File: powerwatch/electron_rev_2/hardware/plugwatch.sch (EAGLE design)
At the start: 86 parts, among them J1 TC2030-JLINK-NL, J2 DM3AT-SF-PEJM5, SW1 SIP3240X, SW2 SIP3240X, SW3 SIP3240X, SW4 SIP3240X, SW7 SIP3240X, U1 MAX-M8, U3 ISL29035, U37 MPU-9250, U4 NRF51822QF, U5 SAFFB1G56KB0F0A, U6 BGA725L6-ALT, U7 OPA322AIDBVT, U8 MAX740XESA, X3 16MHz, X4 ABS05-32.768KHZ-9-T

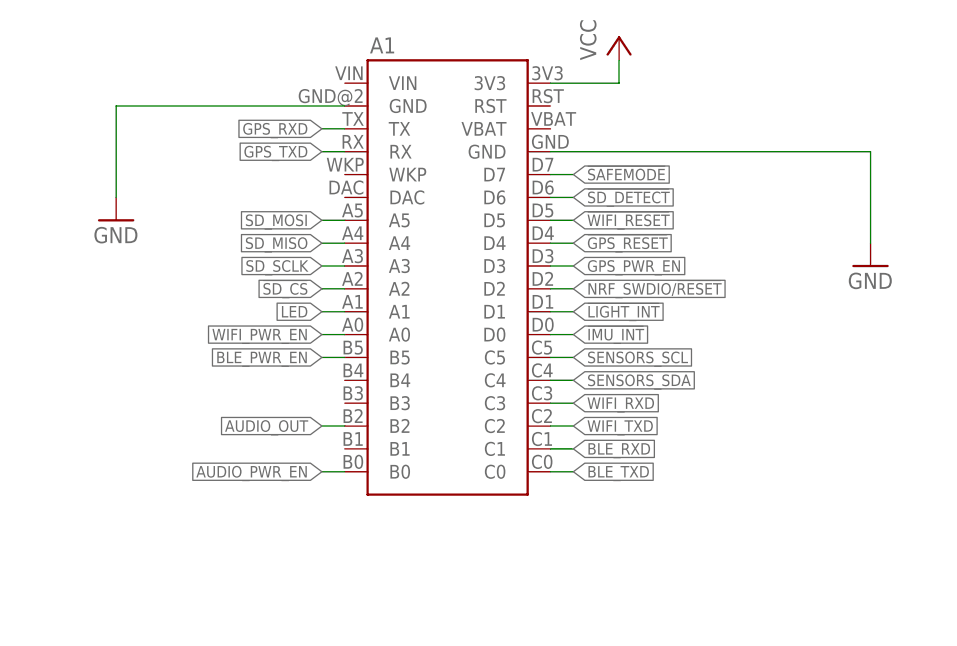
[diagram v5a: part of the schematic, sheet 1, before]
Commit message: Reroute, move signals on Electron
Add names/dates/revision
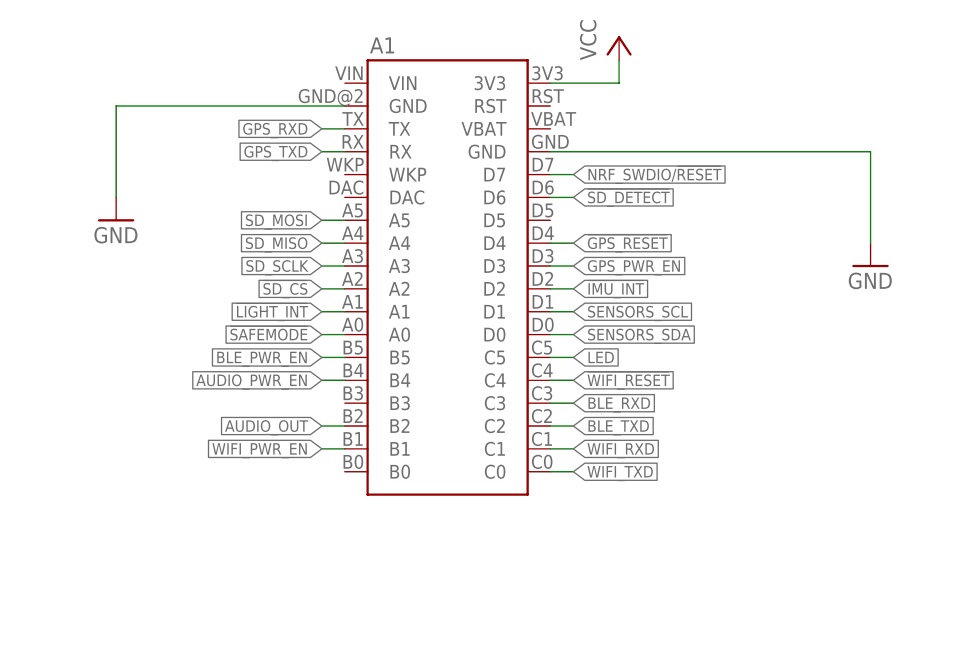
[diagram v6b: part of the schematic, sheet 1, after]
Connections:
- net !IMU_INT: now also A1.D2; no longer A1.D0
- net !LIGHT_INT: now also A1.A1; no longer A1.D1
- net !SAFEMODE: now also A1.A0; no longer A1.D7
- net !WIFI_RESET: now also A1.C4; no longer A1.D5
- net AUDIO_PWR_EN: now also A1.B4; no longer A1.B0
- net BLE_RXD: now also A1.C3; no longer A1.C1
- net BLE_TXD: now also A1.C2; no longer A1.C0
- net GPS_VCC: now also U1.V_BCKP
- net LED: now also A1.C5; no longer A1.A1
- net NRF_SWDIO/!RESET: now also A1.D7; no longer A1.D2
- net SENSORS_SCL: now also A1.D1; no longer A1.C5
- net SENSORS_SDA: now also A1.D0; no longer A1.C4
- net WIFI_PWR_EN: now also A1.B1; no longer A1.A0
- net WIFI_RXD: now also A1.C1; no longer A1.C3
- net WIFI_TXD: now also A1.C0; no longer A1.C2
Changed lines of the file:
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@@
 </segment>
+<segment>
+<wire x1="63.5" y1="119.38" x2="60.96" y2="119.38" width="0.1524" layer="91"/>
+<label x="60.96" y="119.38" size="1.27" layer="95" rot="R180" xref="yes"/>
+<pinref part="A1" gate="A1" pin="A0"/>
+</segment>
+</net>
+<net name="BLE_TXD" class="0">
+<segment>
+<label x="88.9" y="109.22" size="1.27" layer="95" xref="yes"/>
+<pinref part="A1" gate="A1" pin="C2"/>
+<wire x1="88.9" y1="109.22" x2="86.36" y2="109.22" width="0.1524" layer="91"/>
+</segment>
+</net>
+<net name="BLE_RXD" class="0">
+<segment>
+<wire x1="86.36" y1="111.76" x2="88.9" y2="111.76" width="0.1524" layer="91"/>
+<label x="88.9" y="111.76" size="1.27" layer="95" xref="yes"/>
+<pinref part="A1" gate="A1" pin="C3"/>
+</segment>
+</net>
+<net name="WIFI_TXD" class="0">
+<segment>
+<wire x1="86.36" y1="104.14" x2="88.9" y2="104.14" width="0.1524" layer="91"/>
+<label x="88.9" y="104.14" size="1.27" layer="95" xref="yes"/>
+<pinref part="A1" gate="A1" pin="C0"/>
+</segment>
+</net>
+<net name="WIFI_RXD" class="0">
+<segment>
+<label x="88.9" y="106.68" size="1.27" layer="95" xref="yes"/>
+<pinref part="A1" gate="A1" pin="C1"/>
+<wire x1="86.36" y1="106.68" x2="88.9" y2="106.68" width="0.1524" layer="91"/>
+</segment>
+</net>
+<net name="GPS_RXD" class="0">
+<segment>
+<pinref part="A1" gate="A1" pin="TX"/>
+<wire x1="63.5" y1="142.24" x2="60.96" y2="142.24" width="0.1524" layer="91"/>
+<label x="60.96" y="142.24" size="1.27" layer="95" rot="R180" xref="yes"/>
+</segment>
+</net>
+<net name="GPS_TXD" class="0">
+<segment>
+<pinref part="A1" gate="A1" pin="RX"/>
+<wire x1="63.5" y1="139.7" x2="60.96" y2="139.7" width="0.1524" layer="91"/>
+<label x="60.96" y="139.7" size="1.27" layer="95" rot="R180" xref="yes"/>
+</segment>
+</net>
+<net name="SENSORS_SDA" class="0">
+<segment>
+<label x="88.9" y="119.38" size="1.27" layer="95" xref="yes"/>
+<pinref part="A1" gate="A1" pin="D0"/>
+<wire x1="88.9" y1="119.38" x2="86.36" y2="119.38" width="0.1524" layer="91"/>
+</segment>
+</net>
+<net name="SENSORS_SCL" class="0">
+<segment>
+<label x="88.9" y="121.92" size="1.27" layer="95" xref="yes"/>
+<pinref part="A1" gate="A1" pin="D1"/>
+<wire x1="88.9" y1="121.92" x2="86.36" y2="121.92" width="0.1524" layer="91"/>
+</segment>
+</net>
+<net name="!WIFI_RESET" class="0">
+<segment>
+<label x="88.9" y="114.3" size="1.27" layer="95" xref="yes"/>
+<pinref part="A1" gate="A1" pin="C4"/>
+<wire x1="88.9" y1="114.3" x2="86.36" y2="114.3" width="0.1524" layer="91"/>
+</segment>
+</net>
+<net name="!GPS_RESET" class="0">
+<segment>
+<wire x1="86.36" y1="129.54" x2="88.9" y2="129.54" width="0.1524" layer="91"/>
+<label x="88.9" y="129.54" size="1.27" layer="95" xref="yes"/>
+<pinref part="A1" gate="A1" pin="D4"/>
+</segment>
+</net>
+<net name="GPS_PWR_EN" class="0">
+<segment>
+<wire x1="86.36" y1="127" x2="88.9" y2="127" width="0.1524" layer="91"/>
+<label x="88.9" y="127" size="1.27" layer="95" xref="yes"/>
+<pinref part="A1" gate="A1" pin="D3"/>
+</segment>
+</net>
+<net name="NRF_SWDIO/!RESET" class="0">
 <segment>
 <wire x1="86.36" y1="137.16" x2="88.9" y2="137.16" width="0.1524" layer="91"/>
@@
 </segment>
 </net>
-<net name="BLE_TXD" class="0">
-<segment>
-<pinref part="A1" gate="A1" pin="C0"/>
-<wire x1="86.36" y1="104.14" x2="88.9" y2="104.14" width="0.1524" layer="91"/>
-<label x="88.9" y="104.14" size="1.27" layer="95" xref="yes"/>
-</segment>
-</net>
-<net name="BLE_RXD" class="0">
-<segment>
-<pinref part="A1" gate="A1" pin="C1"/>
-<wire x1="86.36" y1="106.68" x2="88.9" y2="106.68" width="0.1524" layer="91"/>
-<label x="88.9" y="106.68" size="1.27" layer="95" xref="yes"/>
-</segment>
-</net>
-<net name="WIFI_TXD" class="0">
-<segment>
-<pinref part="A1" gate="A1" pin="C2"/>
-<wire x1="86.36" y1="109.22" x2="88.9" y2="109.22" width="0.1524" layer="91"/>
-<label x="88.9" y="109.22" size="1.27" layer="95" xref="yes"/>
-</segment>
-</net>
-<net name="WIFI_RXD" class="0">
-<segment>
-<pinref part="A1" gate="A1" pin="C3"/>
-<wire x1="86.36" y1="111.76" x2="88.9" y2="111.76" width="0.1524" layer="91"/>
-<label x="88.9" y="111.76" size="1.27" layer="95" xref="yes"/>
-</segment>
-</net>
-<net name="GPS_RXD" class="0">
-<segment>
-<pinref part="A1" gate="A1" pin="TX"/>
-<wire x1="63.5" y1="142.24" x2="60.96" y2="142.24" width="0.1524" layer="91"/>
-<label x="60.96" y="142.24" size="1.27" layer="95" rot="R180" xref="yes"/>
-</segment>
-</net>
-<net name="GPS_TXD" class="0">
-<segment>
-<pinref part="A1" gate="A1" pin="RX"/>
-<wire x1="63.5" y1="139.7" x2="60.96" y2="139.7" width="0.1524" layer="91"/>
-<label x="60.96" y="139.7" size="1.27" layer="95" rot="R180" xref="yes"/>
-</segment>
-</net>
-<net name="SENSORS_SDA" class="0">
-<segment>
-<pinref part="A1" gate="A1" pin="C4"/>
-<wire x1="86.36" y1="114.3" x2="88.9" y2="114.3" width="0.1524" layer="91"/>
-<label x="88.9" y="114.3" size="1.27" layer="95" xref="yes"/>
-</segment>
-</net>
-<net name="SENSORS_SCL" class="0">
-<segment>
-<pinref part="A1" gate="A1" pin="C5"/>
-<wire x1="86.36" y1="116.84" x2="88.9" y2="116.84" width="0.1524" layer="91"/>
-<label x="88.9" y="116.84" size="1.27" layer="95" xref="yes"/>
-</segment>
-</net>
-<net name="!WIFI_RESET" class="0">
-<segment>
-<wire x1="86.36" y1="132.08" x2="88.9" y2="132.08" width="0.1524" layer="91"/>
-<label x="88.9" y="132.08" size="1.27" layer="95" xref="yes"/>
-<pinref part="A1" gate="A1" pin="D5"/>
-</segment>
-</net>
-<net name="!GPS_RESET" class="0">
-<segment>
-<wire x1="86.36" y1="129.54" x2="88.9" y2="129.54" width="0.1524" layer="91"/>
-<label x="88.9" y="129.54" size="1.27" layer="95" xref="yes"/>
-<pinref part="A1" gate="A1" pin="D4"/>
-</segment>
-</net>
-<net name="GPS_PWR_EN" class="0">
-<segment>
-<wire x1="86.36" y1="127" x2="88.9" y2="127" width="0.1524" layer="91"/>
-<label x="88.9" y="127" size="1.27" layer="95" xref="yes"/>
-<pinref part="A1" gate="A1" pin="D3"/>
-</segment>
-</net>
-<net name="NRF_SWDIO/!RESET" class="0">
+<net name="!LIGHT_INT" class="0">
+<segment>
+<label x="60.96" y="121.92" size="1.27" layer="95" rot="R180" xref="yes"/>
+<pinref part="A1" gate="A1" pin="A1"/>
+<wire x1="63.5" y1="121.92" x2="60.96" y2="121.92" width="0.1524" layer="91"/>
+</segment>
+</net>
+<net name="!IMU_INT" class="0">
 <segment>
 <wire x1="86.36" y1="124.46" x2="88.9" y2="124.46" width="0.1524" layer="91"/>
@@
 </segment>
 </net>
-<net name="!LIGHT_INT" class="0">
-<segment>
-<wire x1="86.36" y1="121.92" x2="88.9" y2="121.92" width="0.1524" layer="91"/>
-<label x="88.9" y="121.92" size="1.27" layer="95" xref="yes"/>
-<pinref part="A1" gate="A1" pin="D1"/>
-</segment>
-</net>
-<net name="!IMU_INT" class="0">
-<segment>
-<wire x1="86.36" y1="119.38" x2="88.9" y2="119.38" width="0.1524" layer="91"/>
-<label x="88.9" y="119.38" size="1.27" layer="95" xref="yes"/>
-<pinref part="A1" gate="A1" pin="D0"/>
-</segment>
-</net>
 <net name="AUDIO_OUT" class="0">
 <segment>
@@
 <net name="AUDIO_PWR_EN" class="0">
 <segment>
-<pinref part="A1" gate="A1" pin="B0"/>
-<wire x1="63.5" y1="104.14" x2="60.96" y2="104.14" width="0.1524" layer="91"/>
-<label x="60.96" y="104.14" size="1.27" layer="95" rot="R180" xref="yes"/>
+<label x="60.96" y="114.3" size="1.27" layer="95" rot="R180" xref="yes"/>
+<pinref part="A1" gate="A1" pin="B4"/>
+<wire x1="60.96" y1="114.3" x2="63.5" y2="114.3" width="0.1524" layer="91"/>
 </segment>
 </net>
@@
 <net name="LED" class="0">
 <segment>
-<pinref part="A1" gate="A1" pin="A1"/>
-<wire x1="63.5" y1="121.92" x2="60.96" y2="121.92" width="0.1524" layer="91"/>
-<label x="60.96" y="121.92" size="1.27" layer="95" rot="R180" xref="yes"/>
+<label x="88.9" y="116.84" size="1.27" layer="95" xref="yes"/>
+<pinref part="A1" gate="A1" pin="C5"/>
+<wire x1="86.36" y1="116.84" x2="88.9" y2="116.84" width="0.1524" layer="91"/>
 </segment>
 <segment>
@@
 <net name="WIFI_PWR_EN" class="0">
 <segment>
-<pinref part="A1" gate="A1" pin="A0"/>
-<wire x1="63.5" y1="119.38" x2="60.96" y2="119.38" width="0.1524" layer="91"/>
-<label x="60.96" y="119.38" size="1.27" layer="95" rot="R180" xref="yes"/>
+<wire x1="63.5" y1="106.68" x2="60.96" y2="106.68" width="0.1524" layer="91"/>
+<label x="60.96" y="106.68" size="1.27" layer="95" rot="R180" xref="yes"/>
+<pinref part="A1" gate="A1" pin="B1"/>
 </segment>
 </net>
@@
 <wire x1="137.16" y1="154.94" x2="134.62" y2="154.94" width="0.1524" layer="91"/>
 <junction x="134.62" y="154.94"/>
-</segment>
-<segment>
+<pinref part="U1" gate="MAX-M8" pin="V_BCKP"/>
+<wire x1="139.7" y1="148.59" x2="139.7" y2="154.94" width="0.1524" layer="91"/>
+<wire x1="139.7" y1="154.94" x2="137.16" y2="154.94" width="0.1524" layer="91"/>
+<junction x="137.16" y="154.94"/>
+</segment>
+<segment>

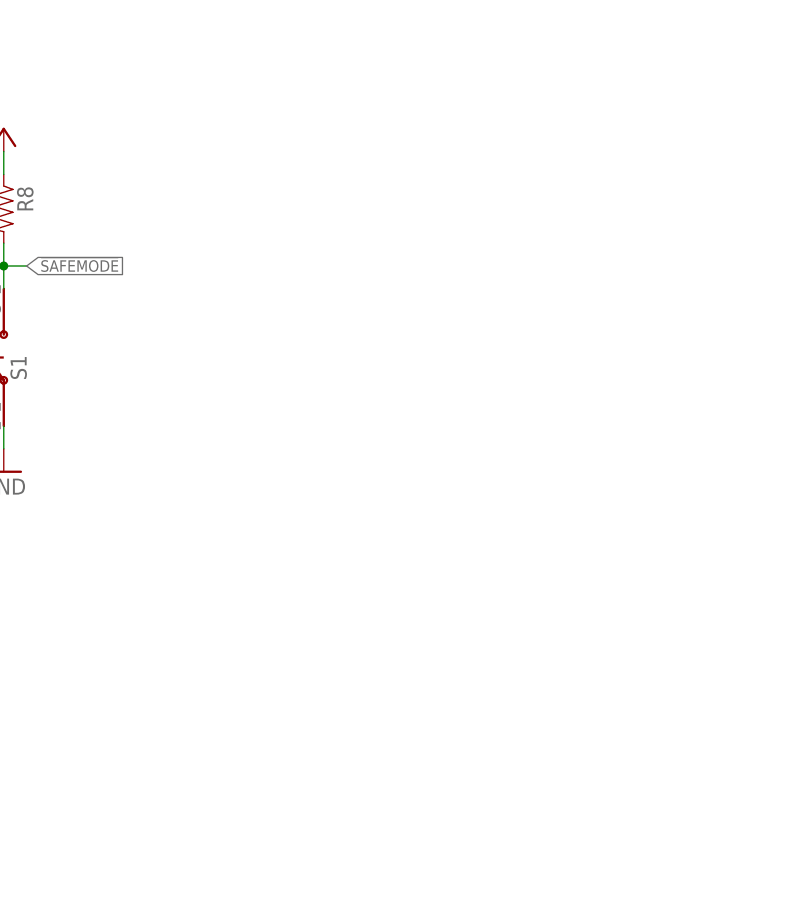
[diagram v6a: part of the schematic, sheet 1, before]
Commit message: Add testpoints
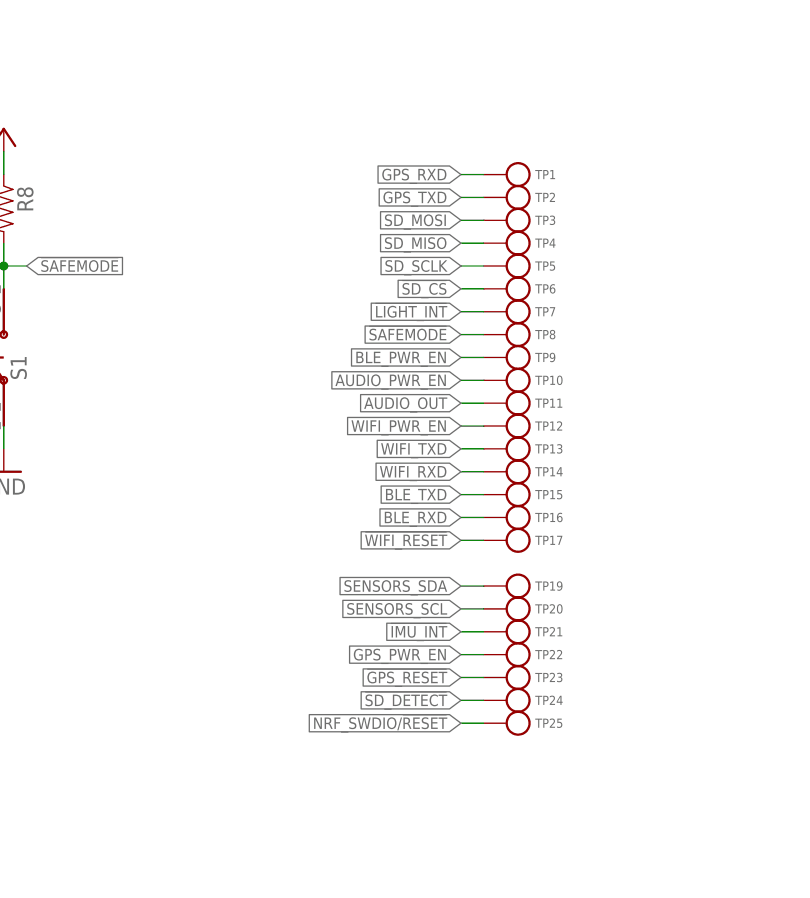
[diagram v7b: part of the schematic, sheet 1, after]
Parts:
- added TP1, TP10, TP11, TP12, TP13, TP14, TP15, TP16, TP17, TP19, TP2, TP20, TP21, TP22, TP23, TP24, TP25, TP3, TP4, TP5, TP6, TP7, TP8, TP9: TEST_POINT_0.040IN, headers:TEST_POINT_0.040IN
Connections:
- net !GPS_RESET: now also TP23.TESTPOINT
- net !IMU_INT: now also TP21.TESTPOINT
- net !LIGHT_INT: now also TP7.TESTPOINT
- net !SAFEMODE: now also TP8.TESTPOINT
- net !SD_CS: now also TP6.TESTPOINT
- net !SD_DETECT: now also TP24.TESTPOINT
- net !WIFI_RESET: now also TP17.TESTPOINT
- net AUDIO_OUT: now also TP11.TESTPOINT
- net AUDIO_PWR_EN: now also TP10.TESTPOINT
- net BLE_PWR_EN: now also TP9.TESTPOINT
- net BLE_RXD: now also TP16.TESTPOINT
- net BLE_TXD: now also TP15.TESTPOINT
- net GPS_PWR_EN: now also TP22.TESTPOINT
- net GPS_RXD: now also TP1.TESTPOINT
- net GPS_TXD: now also TP2.TESTPOINT
- net NRF_SWDIO/!RESET: now also TP25.TESTPOINT
- net SD_MISO: now also TP4.TESTPOINT
- net SD_MOSI: now also TP3.TESTPOINT
- net SD_SCLK: now also TP5.TESTPOINT
- net SENSORS_SCL: now also TP20.TESTPOINT
- net SENSORS_SDA: now also TP19.TESTPOINT
- net WIFI_PWR_EN: now also TP12.TESTPOINT
- net WIFI_RXD: now also TP14.TESTPOINT
- net WIFI_TXD: now also TP13.TESTPOINT

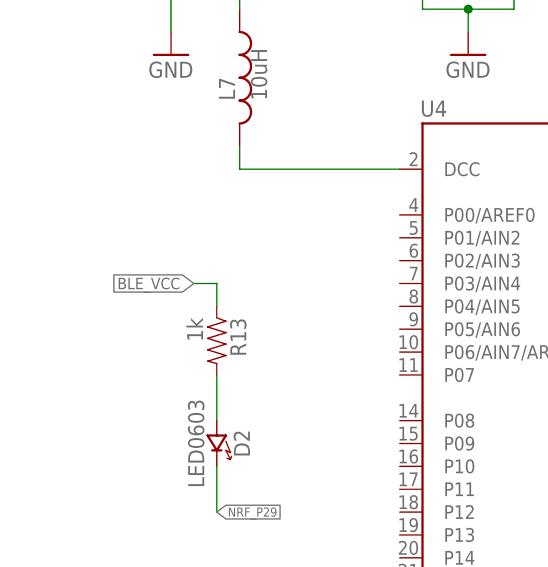
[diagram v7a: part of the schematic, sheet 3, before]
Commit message: Fixed a schematic boo boo
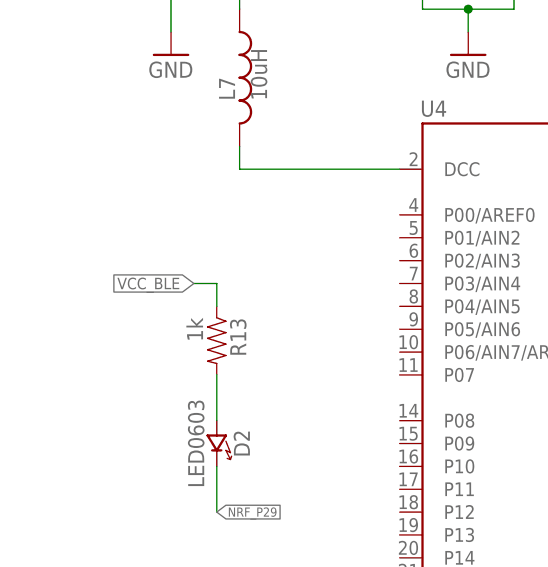
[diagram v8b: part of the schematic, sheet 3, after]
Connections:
- removed net BLE_VCC: R13.1
- net VCC_BLE: now also R13.1
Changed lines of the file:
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@@
 <junction x="114.3" y="167.64"/>
+</segment>
+<segment>
+<pinref part="R13" gate="G$1" pin="1"/>
+<wire x1="33.02" y1="114.3" x2="33.02" y2="116.84" width="0.1524" layer="91"/>
+<label x="30.48" y="116.84" size="1.27" layer="95" rot="R180" xref="yes"/>
+<wire x1="33.02" y1="116.84" x2="30.48" y2="116.84" width="0.1524" layer="91"/>
 </segment>
 </net>
@@
 </segment>
 </net>
-<net name="BLE_VCC" class="0">
-<segment>
-<pinref part="R13" gate="G$1" pin="1"/>
-<wire x1="33.02" y1="114.3" x2="33.02" y2="116.84" width="0.1524" layer="91"/>
-<label x="30.48" y="116.84" size="1.27" layer="95" rot="R180" xref="yes"/>
-<wire x1="33.02" y1="116.84" x2="30.48" y2="116.84" width="0.1524" layer="91"/>
-</segment>
-</net>
